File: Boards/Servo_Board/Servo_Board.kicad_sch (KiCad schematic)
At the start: 47 parts, among them J1 DE9_Pins, J2 Conn_01x03, J3 Conn_01x03, J4 Conn_01x03, J5 Conn_01x03, J6 Conn_01x03, J7 Conn_01x03, J8 Conn_01x03, J9 DE9_Socket, U1 STM32G0B1RCTx, U2 ADP2302ARDZ-5.0, U5 BD50HC5WEFJ-E2, Y2 Crystal 8MHz

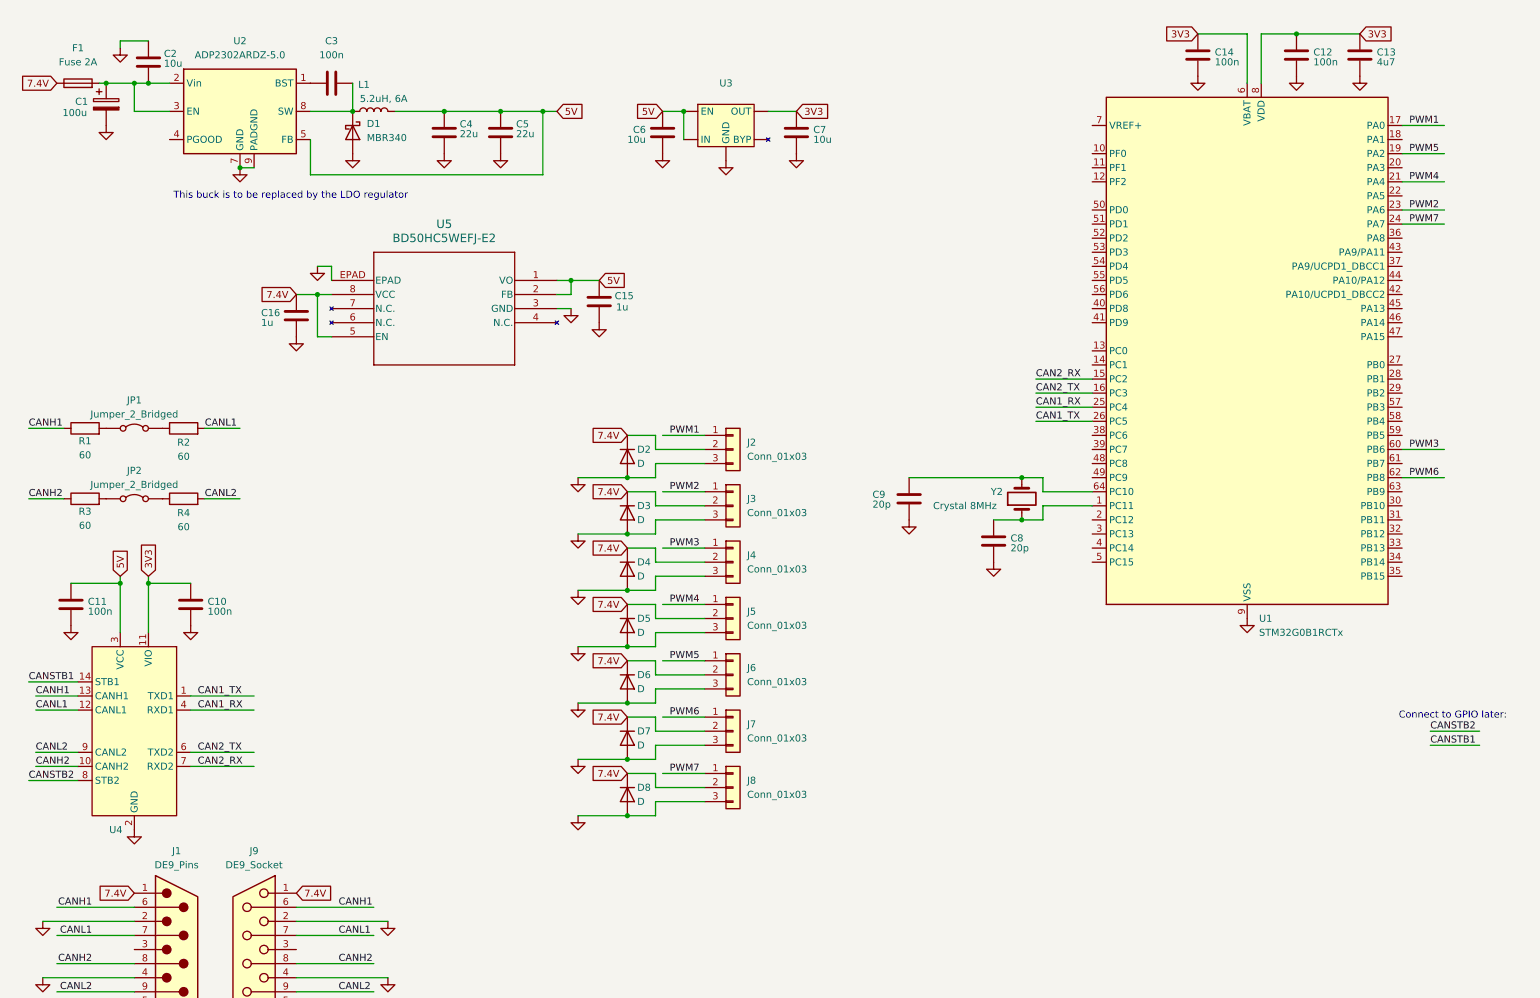
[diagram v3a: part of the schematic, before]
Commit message: Added USB and serial programmer to Servo Board. Added servo feedback lines
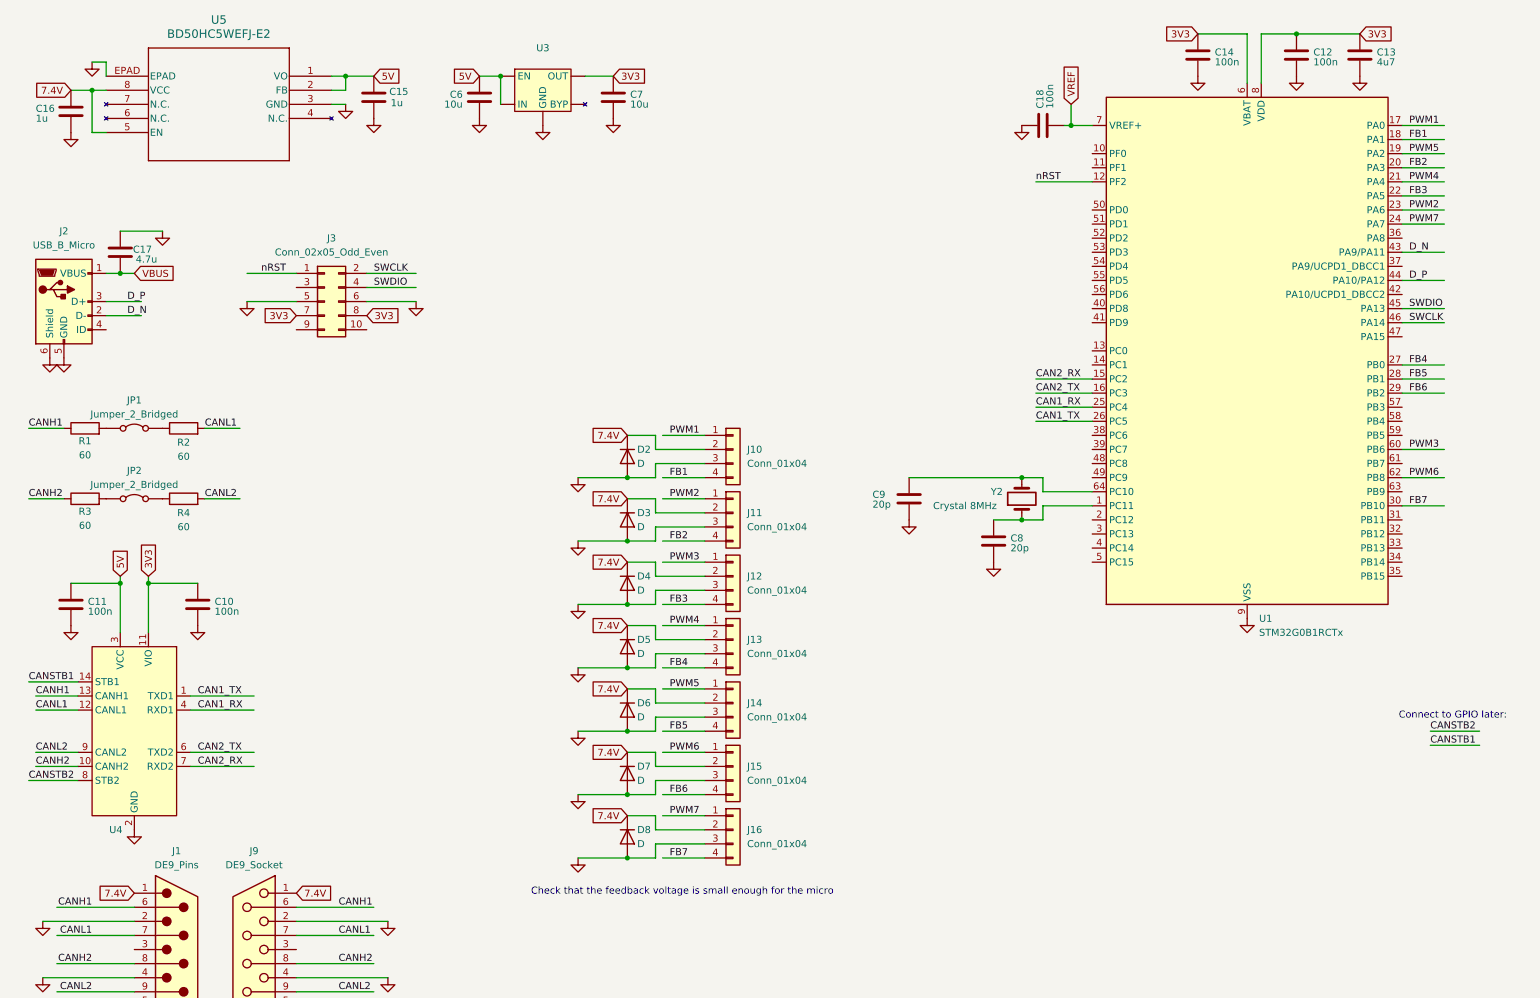
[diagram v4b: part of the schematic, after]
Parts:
- removed C1: 100u, symbol Device:C_Polarized
- removed C2: 10u, symbol Device:C
- removed C3: 100n, symbol Device:C
- removed C4, C5: 22u, symbol Device:C
- removed D1: MBR340, Diode_THT:D_DO-201AD_P15.24mm_Horizontal, symbol Diode:MBR340
- removed F1: Fuse 2A, symbol Device:Fuse
- removed J2, J3, J4, J5, J6, J7, J8: Conn_01x03, symbol Connector_Generic:Conn_01x03
- removed L1: 5.2uH, 6A, symbol Device:L
- removed U2: ADP2302ARDZ-5.0, Package_SO:SOIC-8-1EP_3.9x4.9mm_P1.27mm_EP2.29x3mm, symbol Regulator_Switching:ADP2302ARDZ-5.0
- added C17: 4.7u, symbol Device:C
- added C18: 100n, symbol Device:C
- added J10, J11, J12, J13, J14, J15, J16: Conn_01x04, symbol Connector_Generic:Conn_01x04
- added J2: USB_B_Micro, Connector_USB:USB_Micro-AB_Molex_47590-0001, symbol Connector:USB_B_Micro
- added J3: Conn_02x05_Odd_Even, Connector_IDC:IDC-Header_2x05_P2.54mm_Vertical, symbol Connector_Generic:Conn_02x05_Odd_Even
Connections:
- net 3V3: now also J3.7 (Pin_7), J3.8 (Pin_8)
- net 7.4V: now also J10.2 (Pin_2), J11.2 (Pin_2), J12.2 (Pin_2), J13.2 (Pin_2), J14.2 (Pin_2), J15.2 (Pin_2), J16.2 (Pin_2)
- net GND: now also C17.1, C18.1, J10.3 (Pin_3), J11.3 (Pin_3), J12.3 (Pin_3), J13.3 (Pin_3), J14.3 (Pin_3), J15.3 (Pin_3), J16.3 (Pin_3), J2.5 (GND), J2.6 (Shield), J3.5 (Pin_5), J3.6 (Pin_6)
- net PWM1: now also J10.1 (Pin_1)
- net PWM2: now also J11.1 (Pin_1)
- net PWM3: now also J12.1 (Pin_1)
- net PWM4: now also J13.1 (Pin_1)
- net PWM5: now also J14.1 (Pin_1)
- net PWM6: now also J15.1 (Pin_1)
- net PWM7: now also J16.1 (Pin_1)
- net nRST: now reaches U1.12 (PF2)
- net nRST: now also J3.1 (Pin_1)
- net FB1: now reaches U1.18 (PA1)
- net FB1: now also J10.4 (Pin_4)
- net FB2: now reaches U1.20 (PA3)
- net FB2: now also J11.4 (Pin_4)
- net FB3: now reaches U1.22 (PA5)
- net FB3: now also J12.4 (Pin_4)
- net FB4: now reaches U1.27 (PB0)
- net FB4: now also J13.4 (Pin_4)
- net FB5: now reaches U1.28 (PB1)
- net FB5: now also J14.4 (Pin_4)
- net FB6: now reaches U1.29 (PB2)
- net FB6: now also J15.4 (Pin_4)
- net FB7: now reaches U1.30 (PB10)
- net FB7: now also J16.4 (Pin_4)
- net D_N: now reaches U1.43 (PA9/PA11)
- net D_N: now also J2.2 (D-)
- net D_P: now reaches U1.44 (PA10/PA12)
- net D_P: now also J2.3 (D+)
- net SWDIO: now reaches U1.45 (PA13)
- net SWDIO: now also J3.4 (Pin_4)
- net SWCLK: now reaches U1.46 (PA14)
- net SWCLK: now also J3.2 (Pin_2)
- net VREF: now reaches U1.7 (VREF+)
- net VREF: now also C18.2
- new net VBUS: C17.2, J2.1 (VBUS)
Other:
- note added: "Check that the feedback voltage is small enough for the micro"
- note removed: "This buck is to be replaced by the LDO regulator"
- moved on the sheet: C10, C15, C16, C6, C7, D3, D4, D5, D6, D7, D8, U3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

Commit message: Forgot termination resistors
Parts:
- added R5, R6: 27R, symbol Device:R
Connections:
- net D_N: now also R5.2; no longer U1.43 (PA9/PA11)
- net D_P: now also R6.2; no longer U1.44 (PA10/PA12)
- new net: R5.1, U1.43 (PA9/PA11)
- new net: R6.1, U1.44 (PA10/PA12)
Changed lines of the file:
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@@
 	(wire
 		(pts
-			(xy 261.62 58.42) (xy 269.24 58.42)
-		)
-		(stroke
-			(width 0)
-			(type default)
-		)
-	)
-	(wire
-		(pts
 			(xy 127 128.27) (xy 127 125.73)
 		)
@@
 	(wire
 		(pts
+			(xy 269.24 63.5) (xy 275.59 63.5)
+		)
+		(stroke
+			(width 0)
+			(type default)
+		)
+	)
+	(wire
+		(pts
 			(xy 128.27 114.3) (xy 135.89 114.3)
 		)
@@
 	(wire
 		(pts
+			(xy 269.24 58.42) (xy 275.59 58.42)
+		)
+		(stroke
+			(width 0)
+			(type default)
+		)
+	)
+	(wire
+		(pts
 			(xy 53.34 67.31) (xy 62.23 67.31)
 		)
@@
 	(wire
 		(pts
-			(xy 261.62 63.5) (xy 269.24 63.5)
-		)
-		(stroke
-			(width 0)
-			(type default)
-		)
-	)
-	(wire
-		(pts
 			(xy 127 130.81) (xy 127 133.35)
 		)
@@
 	)
 	(label "D_P"
-		(at 262.89 63.5 0)
+		(at 269.24 63.5 0)
 		(effects
 			(font
@@
 	)
 	(label "D_N"
-		(at 262.89 58.42 0)
+		(at 269.24 58.42 0)
 		(effects
 			(font
@@
 	(symbol
 		(lib_id "Device:R")
+		(at 265.43 58.42 90)
+		(unit 1)
+		(exclude_from_sim no)
+		(in_bom yes)
+		(on_board yes)
+		(dnp no)
+		(property "Reference" "R5"
+			(at 267.462 56.388 90)
+			(effects
+				(font
+					(size 1.27 1.27)
+				)
+			)
+		)
+		(property "Value" "27R"
+			(at 263.906 56.388 90)
+			(effects
+				(font
+					(size 1.27 1.27)
+				)
+			)
+		)
+		(property "Footprint" ""
+			(at 265.43 60.198 90)
+			(effects
+				(font
+					(size 1.27 1.27)
+				)
+				(hide yes)
+			)
+		)
+		(property "Datasheet" "~"
+			(at 265.43 58.42 0)
+			(effects
+				(font
+					(size 1.27 1.27)
+				)
+				(hide yes)
+			)
+		)
+		(property "Description" "Resistor"
+			(at 265.43 58.42 0)
+			(effects
+				(font
+					(size 1.27 1.27)
+				)
+				(hide yes)
+			)
+		)
+		(pin "2"
+		)
+		(pin "1"
+		)
+		(instances
+			(project ""
+				(path "/2ef6413b-3d6c-4280-a117-e3d1b74ccf03"
+					(reference "R5")
+					(unit 1)
+				)
+			)
+		)
+	)
+	(symbol
+		(lib_id "Device:R")
 		(at 41.91 102.87 90)
 		(unit 1)
@@
 					(unit 1)
 				)
+			)
+		)
+	)
+	(symbol
+		(lib_id "Device:R")
+		(at 265.43 63.5 90)
+		(unit 1)
+		(exclude_from_sim no)
+		(in_bom yes)
+		(on_board yes)
+		(dnp no)
+		(property "Reference" "R6"
+			(at 267.462 61.468 90)
+			(effects
+				(font
+					(size 1.27 1.27)
+				)
+			)
+		)
+		(property "Value" "27R"
+			(at 263.906 61.468 90)
+			(effects
+				(font
+					(size 1.27 1.27)
+				)
+			)
+		)
+		(property "Footprint" ""
+			(at 265.43 65.278 90)
+			(effects
+				(font
+					(size 1.27 1.27)
+				)
+				(hide yes)
+			)
+		)
+		(property "Datasheet" "~"
+			(at 265.43 63.5 0)
+			(effects
+				(font
+					(size 1.27 1.27)
+				)
+				(hide yes)
+			)
+		)
+		(property "Description" "Resistor"
+			(at 265.43 63.5 0)
+			(effects
+				(font
+					(size 1.27 1.27)
+				)
+				(hide yes)
+			)
+		)
+		(pin "2"
+		)
+		(pin "1"
+		)
+		(instances
+			(project "Servo_Board"
+				(path "/2ef6413b-3d6c-4280-a117-e3d1b74ccf03"
+					(reference "R6")
+					(unit 1)
+				)

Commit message: Finished Servo board and ADC board for review tomorrow
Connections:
- net CANSTB1: now also U1.32 (PB12)
- net CANSTB2: now also U1.31 (PB11)
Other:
- note removed: "Connect to GPIO later:"
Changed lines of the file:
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@@
-		)
-	)
-	(text "Connect to GPIO later:"
-		(exclude_from_sim no)
-		(at 270.764 141.986 0)
-		(effects
-			(font
-				(size 1.27 1.27)
-			)
 		)
 	)
@@
 	(wire
 		(pts
+			(xy 261.62 106.68) (xy 271.78 106.68)
+		)
+		(stroke
+			(width 0)
+			(type default)
+		)
+	)
+	(wire
+		(pts
 			(xy 33.02 62.23) (xy 30.48 62.23)
 		)
@@
 	(wire
 		(pts
-			(xy 266.7 147.32) (xy 275.59 147.32)
-		)
-		(stroke
-			(width 0)
-			(type default)
-		)
-	)
-	(wire
-		(pts
 			(xy 71.12 31.75) (xy 68.58 31.75)
 		)
@@
 	(wire
 		(pts
+			(xy 261.62 109.22) (xy 271.78 109.22)
+		)
+		(stroke
+			(width 0)
+			(type default)
+		)
+	)
+	(wire
+		(pts
 			(xy 233.68 19.05) (xy 233.68 27.94)
 		)
@@
 		(pts
 			(xy 15.24 140.97) (xy 22.86 140.97)
-		)
-		(stroke
-			(width 0)
-			(type default)
-		)
-	)
-	(wire
-		(pts
-			(xy 266.7 144.78) (xy 275.59 144.78)
 		)
 		(stroke
@@
 	)
 	(label "CANSTB2"
-		(at 266.7 144.78 0)
+		(at 262.89 106.68 0)
 		(effects
 			(font
@@
 	)
 	(label "CANSTB1"
-		(at 266.7 147.32 0)
-		(effects
-			(font
+		(at 262.89 109.22 0)
+		(effects
+			(font

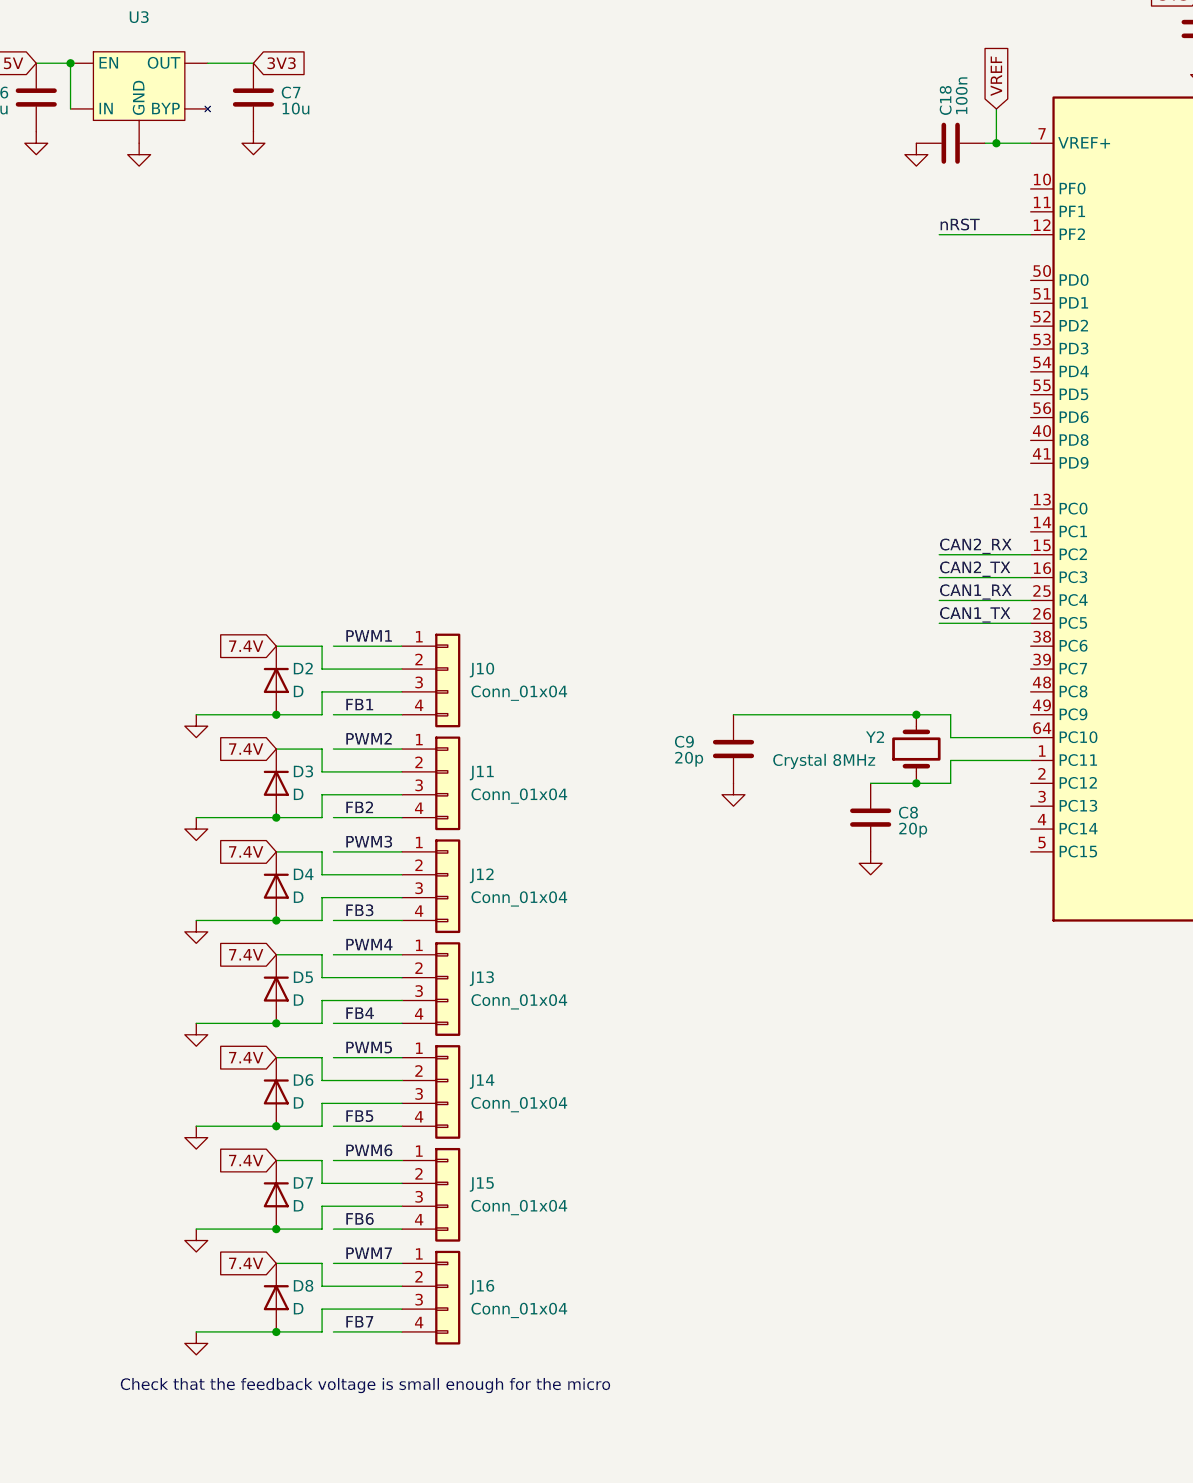
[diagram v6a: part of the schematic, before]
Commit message: Footprints for the servo and ADC board
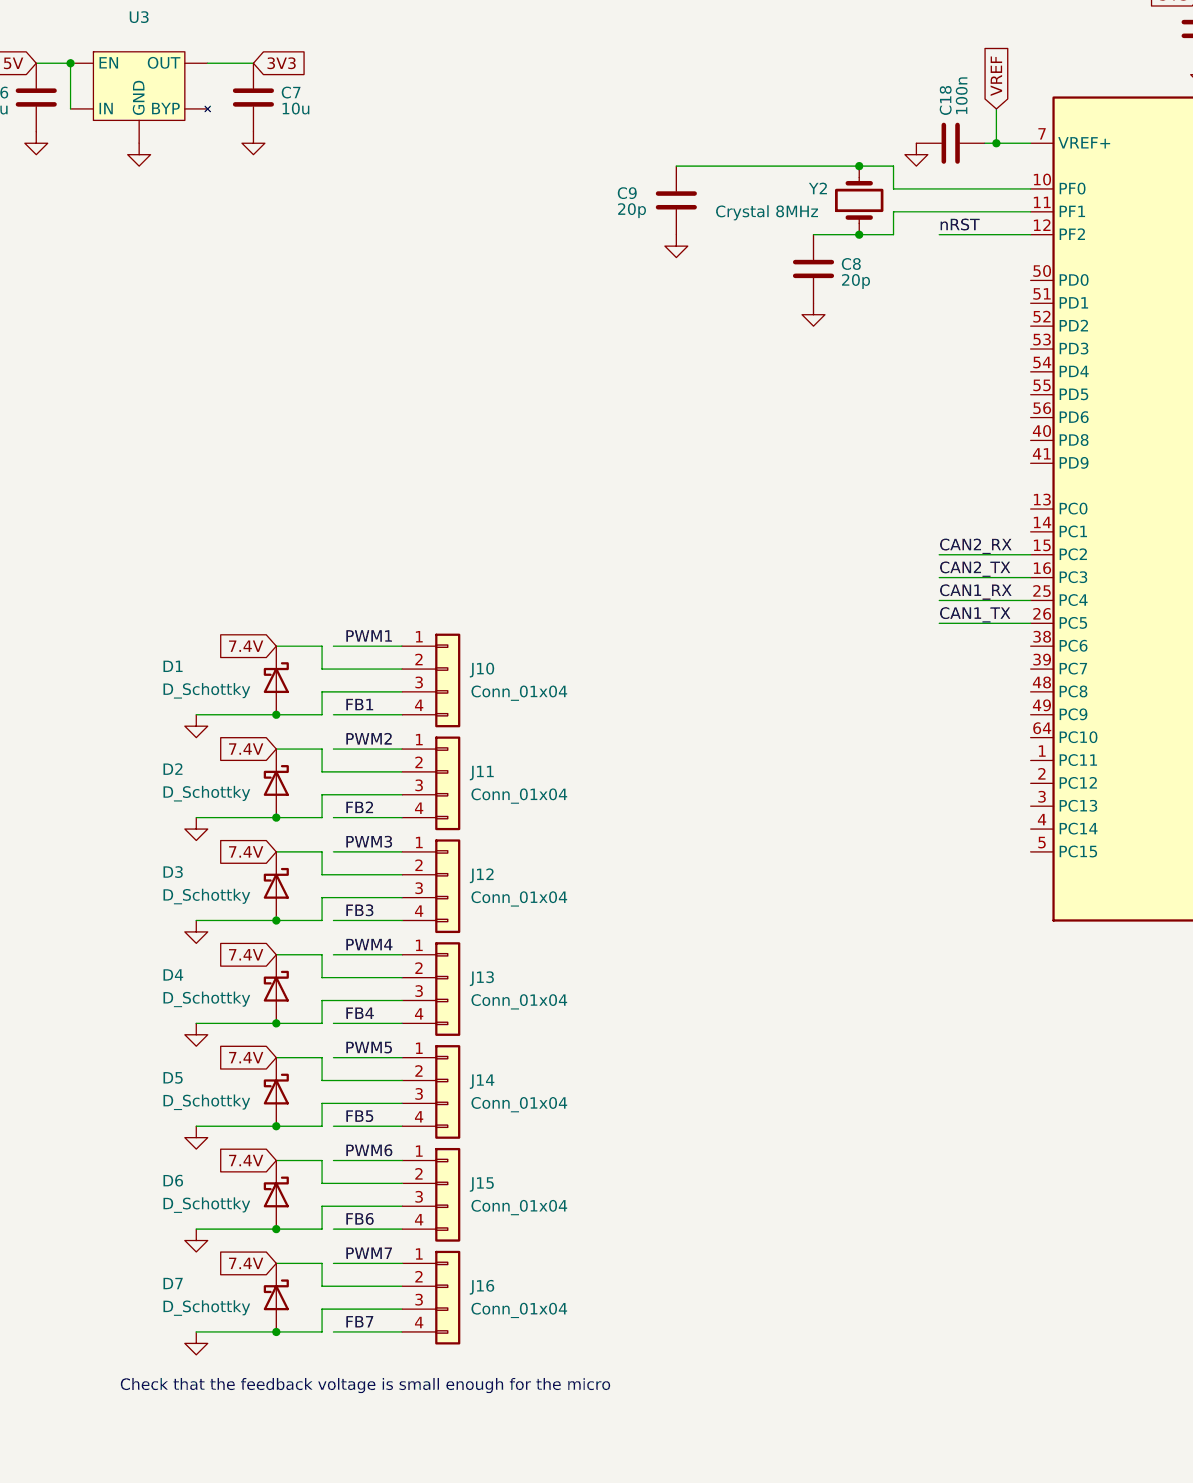
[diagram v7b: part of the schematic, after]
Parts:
- removed D2, D3, D4, D5, D6, D7, D8: D, symbol Device:D
- added D1, D2, D3, D4, D5, D6, D7: D_Schottky, Diode_SMD:D_SOD-882, symbol Device:D_Schottky
- C10, C11, C12, C13, C14, C15, C16, C17, C18, C6, C7, C8, C9: footprint (none) -> Capacitor_SMD:C_0603_1608Metric
- J1, J9: footprint (none) -> Connector_Molex:Molex_Micro-Fit_3.0_43650-0915_1x09_P3.00mm_Vertical; MPN (none) -> 0436500916; Part Number (none) -> 0436500916
- J10, J11, J12, J13, J14, J15, J16: footprint (none) -> Connector_Molex:Molex_Micro-Fit_3.0_43045-0412_2x02_P3.00mm_Vertical; MPN (none) -> 0430450428
- JP1, JP2: footprint (none) -> Connector_PinSocket_2.54mm:PinSocket_1x02_P2.54mm_Vertical
- R1, R2, R3, R4, R5, R6: footprint (none) -> Resistor_SMD:R_0603_1608Metric
- U3: footprint (none) -> footprints:TSOT23-5_ONS
- U4: footprint Custom:SOT23_DYY_TEX -> footprints:SOT23_DYY_TEX
- U5: footprint HTSOP-J8_ROM -> footprints:HTSOP-J8_ROM
- Y2: footprint (none) -> Crystal:Crystal_SMD_Abracon_ABM3B-4Pin_5.0x3.2mm
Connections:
- net 7.4V: now also D1.1 (K), D2.1 (K), D3.1 (K), D4.1 (K), D5.1 (K), D6.1 (K), D7.1 (K)
- net GND: now also D1.2 (A), D2.2 (A), D3.2 (A), D4.2 (A), D5.2 (A), D6.2 (A), D7.2 (A)
- net at C9.1, Y2.2: now also U1.10 (PF0); no longer U1.64 (PC10)
- net at C8.1, Y2.1: now also U1.11 (PF1); no longer U1.1 (PC11)
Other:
- moved on the sheet: C8, C9, Y2
